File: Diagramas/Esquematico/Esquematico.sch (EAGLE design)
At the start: 48 parts, among them IC3 DS3231N_DIP, IC4 3071_SMD, J1 Modulo Pir, J2 RASPBERRYPI-40-PIN-GPIO_SMT, K1 SRD-05VDC-SL-C, K2 SRD-05VDC-SL-C, K3 SRD-05VDC-SL-C, K4 SRD-05VDC-SL-C, U1 RFM69HW-868S2

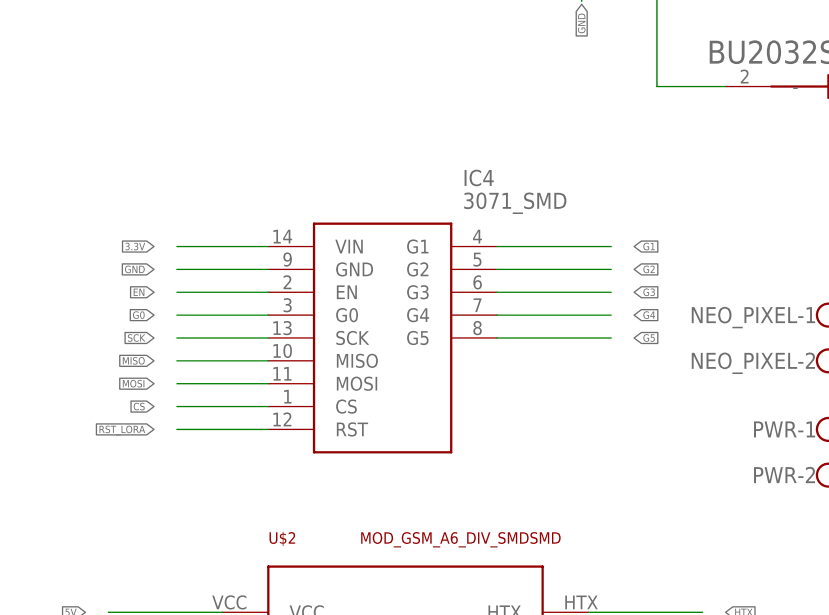
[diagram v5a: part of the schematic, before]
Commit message: Modulo Lora Eliminado
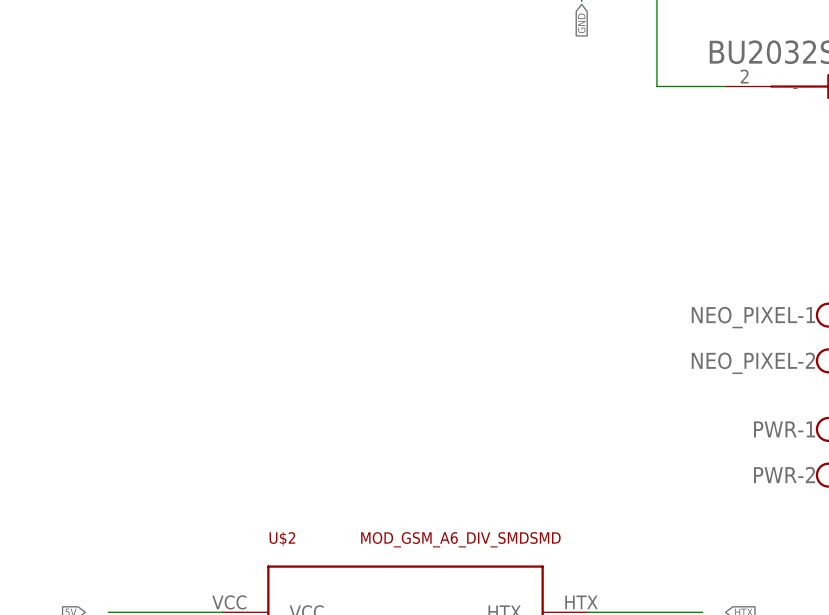
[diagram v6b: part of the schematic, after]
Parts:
- removed IC4: 3071_SMD, 3071:3071_SMD
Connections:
- net 3.3V: no longer IC4.VIN
- net CS: no longer IC4.CS
- net EN: no longer IC4.EN
- net G0: no longer IC4.G0
- net G1: no longer IC4.G1
- net G2: no longer IC4.G2
- net G3: no longer IC4.G3
- net G4: no longer IC4.G4
- net G5: no longer IC4.G5
- net GND: no longer IC4.GND
- net MISO: no longer IC4.MISO
- net MOSI: no longer IC4.MOSI
- net RST_LORA: no longer IC4.RST
- net SCK: no longer IC4.SCK
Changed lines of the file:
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@@
 <layers>
 <layer number="1" name="Top" color="4" fill="1" visible="no" active="no"/>
+<layer number="2" name="Route2" color="1" fill="3" visible="no" active="no"/>
+<layer number="3" name="Route3" color="4" fill="3" visible="no" active="no"/>
+<layer number="4" name="Route4" color="1" fill="4" visible="no" active="no"/>
+<layer number="5" name="Route5" color="4" fill="4" visible="no" active="no"/>
+<layer number="6" name="Route6" color="1" fill="8" visible="no" active="no"/>
+<layer number="7" name="Route7" color="4" fill="8" visible="no" active="no"/>
+<layer number="8" name="Route8" color="1" fill="2" visible="no" active="no"/>
+<layer number="9" name="Route9" color="4" fill="2" visible="no" active="no"/>
+<layer number="10" name="Route10" color="1" fill="7" visible="no" active="no"/>
+<layer number="11" name="Route11" color="4" fill="7" visible="no" active="no"/>
+<layer number="12" name="Route12" color="1" fill="5" visible="no" active="no"/>
+<layer number="13" name="Route13" color="4" fill="5" visible="no" active="no"/>
+<layer number="14" name="Route14" color="1" fill="6" visible="no" active="no"/>
+<layer number="15" name="Route15" color="4" fill="6" visible="no" active="no"/>
 <layer number="16" name="Bottom" color="1" fill="1" visible="no" active="no"/>
 <layer number="17" name="Pads" color="2" fill="1" visible="no" active="no"/>
@@
 <part name="NEO_PIXEL" library="con-wago-500" library_urn="urn:adsk.eagle:library:195" deviceset="W237-102" device="" package3d_urn="urn:adsk.eagle:package:10688/1"/>
 <part name="U$2" library="GPRS_A6 Mini" deviceset="MOD_GSM_A6_DIV_SMD" device="SMD"/>
-<part name="IC4" library="3071" deviceset="3071_SMD" device=""/>
 <part name="J2" library="SparkFun-Connectors" library_urn="urn:adsk.eagle:library:513" deviceset="RASPBERRYPI-40-PIN-GPIO" device="_SMT" package3d_urn="urn:adsk.eagle:package:38280/1"/>
 <part name="BT2" library="BU2032SM-BT-GTR" deviceset="BU2032SM-BT-GTR" device=""/>
@@
 <attribute name="NAME" x="-160.02" y="195.58" size="1.27" layer="94"/>
 <attribute name="VALUE" x="-149.86" y="195.58" size="1.27" layer="94"/>
-</instance>
-<instance part="IC4" gate="G$1" x="-160.02" y="228.6" smashed="yes">
-<attribute name="NAME" x="-138.43" y="236.22" size="1.778" layer="95" align="center-left"/>
-<attribute name="VALUE" x="-138.43" y="233.68" size="1.778" layer="96" align="center-left"/>
 </instance>
 <instance part="J2" gate="G$1" x="-10.16" y="175.26" smashed="yes">
@@
 </segment>
 <segment>
-<pinref part="IC4" gate="G$1" pin="GND"/>
-<wire x1="-160.02" y1="226.06" x2="-170.18" y2="226.06" width="0.1524" layer="91"/>
-<label x="-172.72" y="226.06" size="0.8128" layer="95" rot="R180" xref="yes"/>
-</segment>
-<segment>
 <pinref part="U$2" gate="G$1" pin="GND"/>
 <wire x1="-124.46" y1="177.8" x2="-111.76" y2="177.8" width="0.1524" layer="91"/>
@@
 </segment>
 <segment>
-<pinref part="IC4" gate="G$1" pin="VIN"/>
-<wire x1="-160.02" y1="228.6" x2="-170.18" y2="228.6" width="0.1524" layer="91"/>
-<label x="-172.72" y="228.6" size="0.8128" layer="95" rot="R180" xref="yes"/>
-</segment>
-<segment>
 <pinref part="J2" gate="G$1" pin="3.3V@1"/>
 <wire x1="-25.4" y1="195.58" x2="-38.1" y2="195.58" width="0.1524" layer="91"/>
@@
 </segment>
 <segment>
-<pinref part="IC4" gate="G$1" pin="G1"/>
-<wire x1="-134.62" y1="228.6" x2="-121.92" y2="228.6" width="0.1524" layer="91"/>
-<label x="-119.38" y="228.6" size="0.8128" layer="95" xref="yes"/>
-</segment>
-<segment>
 <pinref part="J2" gate="G$1" pin="GP17"/>
 <wire x1="5.08" y1="167.64" x2="17.78" y2="167.64" width="0.1524" layer="91"/>
@@
 </segment>
 <segment>
-<pinref part="IC4" gate="G$1" pin="G2"/>
-<wire x1="-134.62" y1="226.06" x2="-121.92" y2="226.06" width="0.1524" layer="91"/>
-<label x="-119.38" y="226.06" size="0.8128" layer="95" xref="yes"/>
-</segment>
-<segment>
 <pinref part="J2" gate="G$1" pin="GP24"/>
 <wire x1="5.08" y1="157.48" x2="17.78" y2="157.48" width="0.1524" layer="91"/>
@@
 </segment>
 <segment>
-<pinref part="IC4" gate="G$1" pin="G3"/>
-<wire x1="-134.62" y1="223.52" x2="-121.92" y2="223.52" width="0.1524" layer="91"/>
-<label x="-119.38" y="223.52" size="0.8128" layer="95" xref="yes"/>
-</segment>
-<segment>
 <pinref part="J2" gate="G$1" pin="CE1"/>
 <wire x1="5.08" y1="175.26" x2="17.78" y2="175.26" width="0.1524" layer="91"/>
@@
 <label x="-121.92" y="106.68" size="0.8128" layer="95" xref="yes"/>
 </segment>
-<segment>
-<pinref part="IC4" gate="G$1" pin="G4"/>
-<wire x1="-134.62" y1="220.98" x2="-121.92" y2="220.98" width="0.1524" layer="91"/>
-<label x="-119.38" y="220.98" size="0.8128" layer="95" xref="yes"/>
-</segment>
 </net>
 <net name="G5" class="0">
@@
 <label x="-121.92" y="104.14" size="0.8128" layer="95" xref="yes"/>
 </segment>
-<segment>
-<pinref part="IC4" gate="G$1" pin="G5"/>
-<wire x1="-134.62" y1="218.44" x2="-121.92" y2="218.44" width="0.1524" layer="91"/>
-<label x="-119.38" y="218.44" size="0.8128" layer="95" xref="yes"/>
-</segment>
 </net>
 <net name="CS" class="0">
@@
 <label x="-177.8" y="119.38" size="0.8128" layer="95" rot="R180" xref="yes"/>
 </segment>
-<segment>
-<pinref part="IC4" gate="G$1" pin="CS"/>
-<wire x1="-160.02" y1="210.82" x2="-170.18" y2="210.82" width="0.1524" layer="91"/>
-<label x="-172.72" y="210.82" size="0.8128" layer="95" rot="R180" xref="yes"/>
-</segment>
 </net>
 <net name="MOSI" class="0">
@@
 </segment>
 <segment>
-<pinref part="IC4" gate="G$1" pin="MOSI"/>
-<wire x1="-160.02" y1="213.36" x2="-170.18" y2="213.36" width="0.1524" layer="91"/>
-<label x="-172.72" y="213.36" size="0.8128" layer="95" rot="R180" xref="yes"/>
-</segment>
-<segment>
 <pinref part="J2" gate="G$1" pin="MOSI"/>
 <wire x1="5.08" y1="180.34" x2="17.78" y2="180.34" width="0.1524" layer="91"/>
@@
 </segment>
 <segment>
-<pinref part="IC4" gate="G$1" pin="MISO"/>
-<wire x1="-160.02" y1="215.9" x2="-170.18" y2="215.9" width="0.1524" layer="91"/>
-<label x="-172.72" y="215.9" size="0.8128" layer="95" rot="R180" xref="yes"/>
-</segment>
-<segment>
 <pinref part="J2" gate="G$1" pin="MISO"/>
 <wire x1="5.08" y1="182.88" x2="17.78" y2="182.88" width="0.1524" layer="91"/>
@@
 </segment>
 <segment>
-<pinref part="IC4" gate="G$1" pin="SCK"/>
-<wire x1="-160.02" y1="218.44" x2="-170.18" y2="218.44" width="0.1524" layer="91"/>
-<label x="-172.72" y="218.44" size="0.8128" layer="95" rot="R180" xref="yes"/>
-</segment>
-<segment>
 <pinref part="J2" gate="G$1" pin="SCLK"/>
 <wire x1="5.08" y1="185.42" x2="17.78" y2="185.42" width="0.1524" layer="91"/>
@@
 </segment>
 <segment>
-<pinref part="IC4" gate="G$1" pin="G0"/>
-<wire x1="-160.02" y1="220.98" x2="-170.18" y2="220.98" width="0.1524" layer="91"/>
-<label x="-172.72" y="220.98" size="0.8128" layer="95" rot="R180" xref="yes"/>
-</segment>
-<segment>
 <pinref part="J2" gate="G$1" pin="GP4"/>
 <wire x1="5.08" y1="170.18" x2="17.78" y2="170.18" width="0.1524" layer="91"/>
@@
 </net>
 <net name="EN" class="0">
-<segment>
-<pinref part="IC4" gate="G$1" pin="EN"/>
-<wire x1="-160.02" y1="223.52" x2="-170.18" y2="223.52" width="0.1524" layer="91"/>
-<label x="-172.72" y="223.52" size="0.8128" layer="95" rot="R180" xref="yes"/>
-</segment>
 <segment>
 <pinref part="J2" gate="G$1" pin="CE0"/>
@@
 </segment>
 <segment>
-<pinref part="IC4" gate="G$1" pin="RST"/>
-<wire x1="-160.02" y1="208.28" x2="-170.18" y2="208.28" width="0.1524" layer="91"/>
-<label x="-172.72" y="208.28" size="0.8128" layer="95" rot="R180" xref="yes"/>
-</segment>
-<segment>

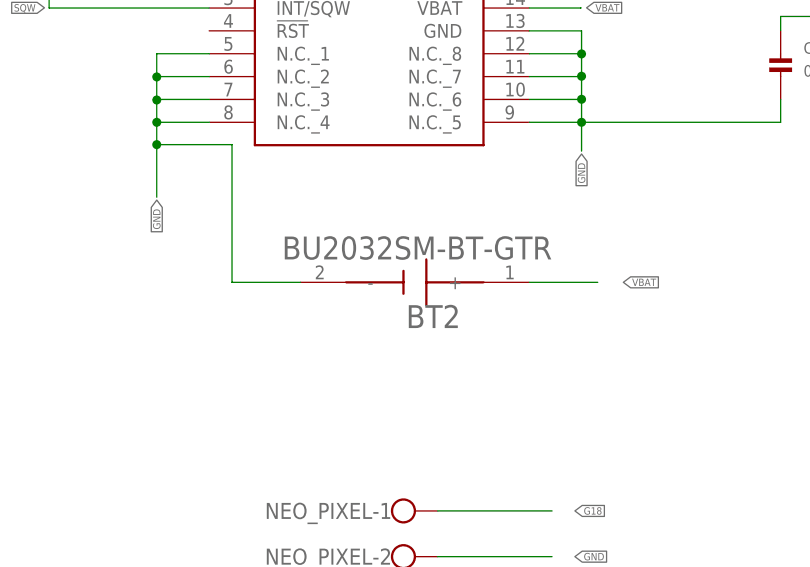
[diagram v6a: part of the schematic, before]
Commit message: Sustitucion de la Bateria
Cambio de la bateria CR2032 por CR1220
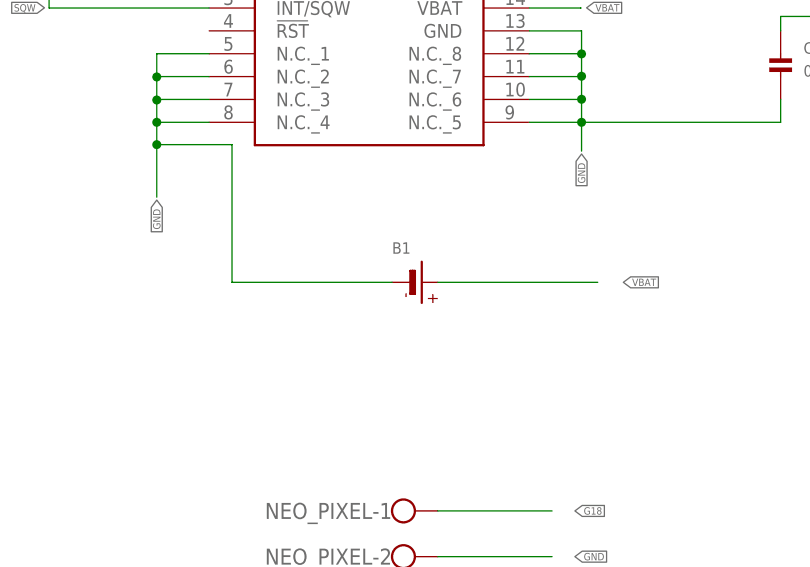
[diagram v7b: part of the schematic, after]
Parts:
- removed BT2: BU2032SM-BT-GTR, BU2032SM-BT-GTR:BU2032SM-BT-GTR
- added B1: (no value), microbuilder:BATTERYCR1220_SMT
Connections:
- net GND: now also B1.-; no longer BT2.-
- net VBAT: now also B1.+; no longer BT2.+
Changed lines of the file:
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@@
 <part name="U$2" library="GPRS_A6 Mini" deviceset="MOD_GSM_A6_DIV_SMD" device="SMD"/>
 <part name="J2" library="SparkFun-Connectors" library_urn="urn:adsk.eagle:library:513" deviceset="RASPBERRYPI-40-PIN-GPIO" device="_SMT" package3d_urn="urn:adsk.eagle:package:38280/1"/>
-<part name="BT2" library="BU2032SM-BT-GTR" deviceset="BU2032SM-BT-GTR" device=""/>
+<part name="B1" library="microbuilder" deviceset="BATTERY" device="CR1220_SMT"/>
 </parts>
 <sheets>
@@
 <attribute name="VALUE" x="-22.86" y="139.7" size="1.778" layer="96"/>
 </instance>
-<instance part="BT2" gate="G$1" x="-96.52" y="246.38" smashed="yes" rot="R180">
-<attribute name="NAME" x="-91.439209375" y="243.839609375" size="2.540390625" layer="95" rot="R180"/>
-<attribute name="VALUE" x="-81.274040625" y="251.465959375" size="2.54298125" layer="96" rot="R180"/>
+<instance part="B1" gate="G$1" x="-96.52" y="246.38" smashed="yes">
+<attribute name="NAME" x="-99.06" y="249.555" size="1.27" layer="95"/>
+<attribute name="VALUE" x="-99.06" y="241.3" size="1.27" layer="96"/>
 </instance>
 </instances>
@@
 <wire x1="-116.84" y1="261.68" x2="-125.2" y2="261.68" width="0.1524" layer="91"/>
 <junction x="-125.2" y="261.68"/>
-<pinref part="BT2" gate="G$1" pin="-"/>
-<wire x1="-109.22" y1="246.38" x2="-116.84" y2="246.38" width="0.1524" layer="91"/>
+<pinref part="B1" gate="G$1" pin="-"/>
+<wire x1="-99.06" y1="246.38" x2="-116.84" y2="246.38" width="0.1524" layer="91"/>
 </segment>
 <segment>
@@
 <segment>
 <label x="-73.36" y="246.38" size="0.8128" layer="95" xref="yes"/>
-<pinref part="BT2" gate="G$1" pin="+"/>
-<wire x1="-83.82" y1="246.38" x2="-76.2" y2="246.38" width="0.1524" layer="91"/>
-</segment>
-<segment>
+<pinref part="B1" gate="G$1" pin="+"/>
+<wire x1="-93.98" y1="246.38" x2="-76.2" y2="246.38" width="0.1524" layer="91"/>
+</segment>
+<segment>

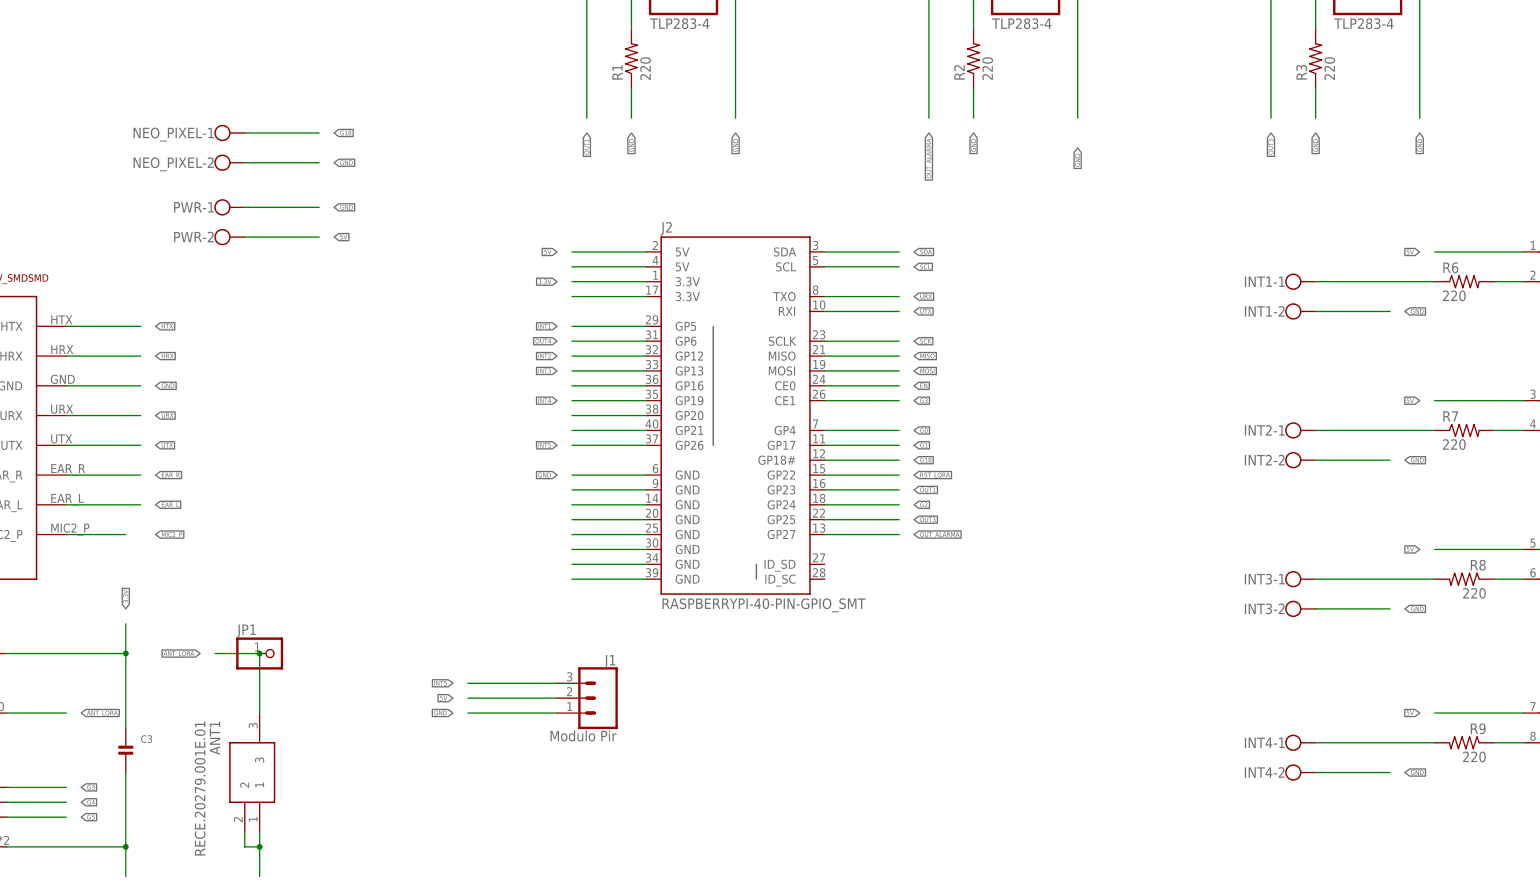
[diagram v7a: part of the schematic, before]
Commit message: Modificaciòn del tamaño de la pcb
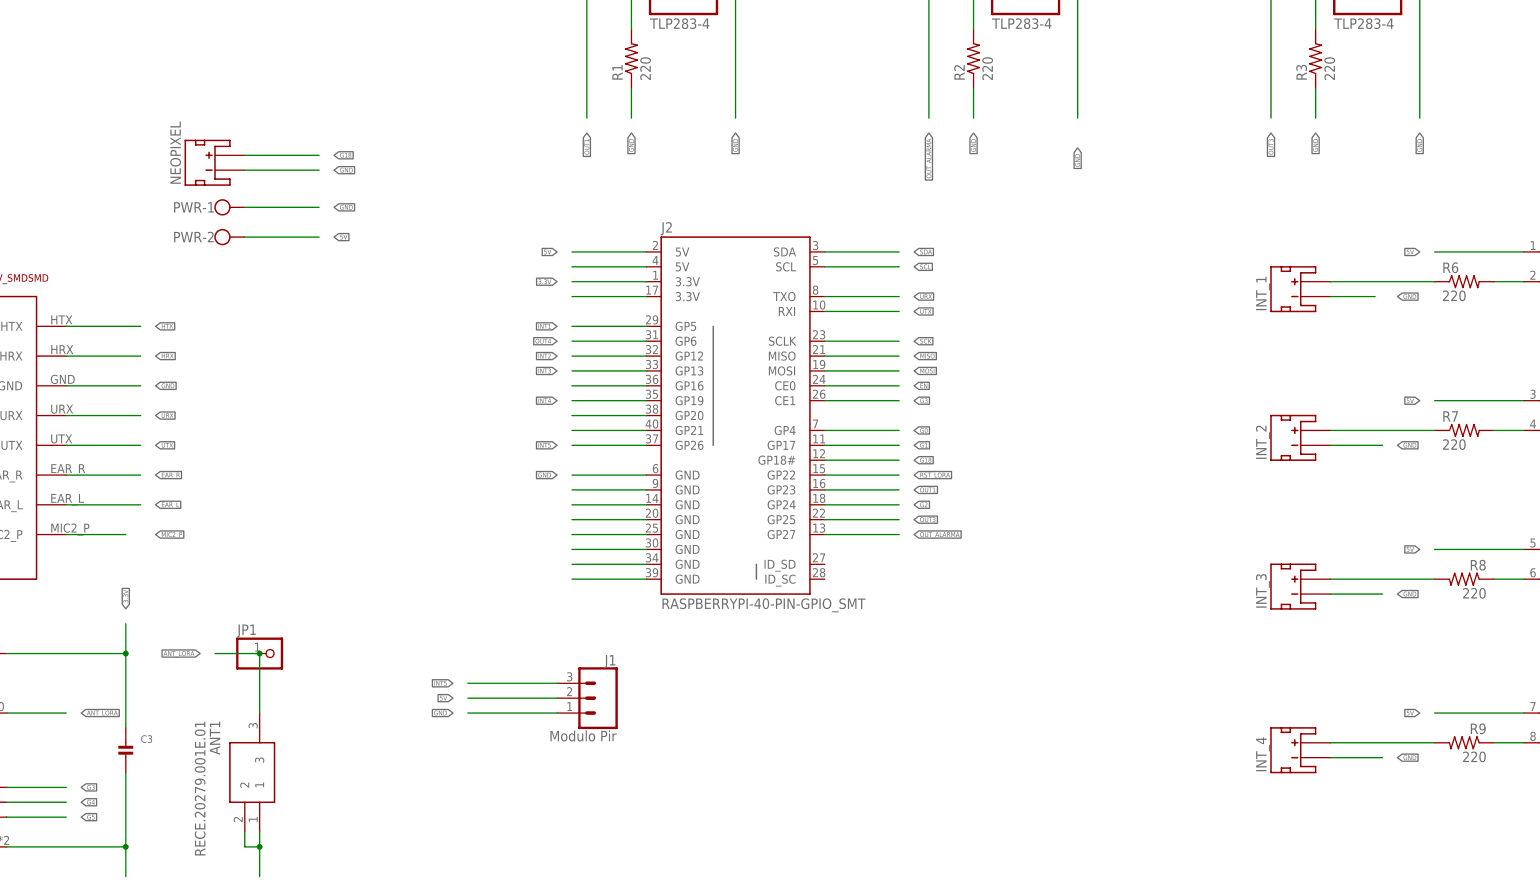
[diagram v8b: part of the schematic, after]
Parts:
- removed INT1, INT2, INT3, INT4, NEO_PIXEL: (no value), con-wago-500:W237-102
- added INT_1, INT_2, INT_3, INT_4, NEOPIXEL: (no value), SparkFun-Connectors:JST_2MM_MALE
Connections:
- net G18: now also NEOPIXEL.+; no longer NEO_PIXEL-1.KL
- net GND: now also INT_1.-, INT_2.-, INT_3.-, INT_4.-, NEOPIXEL.-; no longer INT1-2.KL, INT2-2.KL, INT3-2.KL, INT4-2.KL, NEO_PIXEL-2.KL
- net N$18: now also INT_3.+; no longer INT3-1.KL
- net N$28: now also INT_4.+; no longer INT4-1.KL
- net N$3: now also INT_1.+; no longer INT1-1.KL
- net N$9: now also INT_2.+; no longer INT2-1.KL
